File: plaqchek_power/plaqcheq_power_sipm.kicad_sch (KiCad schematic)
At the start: 20 parts

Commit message: finish schematic
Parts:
- removed U17: ~, symbol plaqchek_mlb:LM5157
- added R23 (x3): 0R, symbol Device:R_Small_US
- added TP3, TP4: TestPoint, symbol Connector:TestPoint
- added U1: LM5157, symbol plaqchek:LM5157
- R37: value 90.9kR -> 110kR
- R41: value 374R -> 464R
- R42: value 374R -> 5.1R
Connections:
- net +12V: now also R23.2; no longer C47.1, C48.2, L4.1, R43.2
- net GND: now also U1.1 (PGND), U1.16 (PGND), U1.17 (EP), U1.7 (AGND)
- net PD_BOOST_PGOOD: now also U1.4 (PGOOD)
- net PD_EN: now also R23.2
- net at R42.2: now also U1.2 (VCC)
- net at R46.2: now also U1.5 (RT)
- net at D2.2 (A), L4.2: now also U1.12 (SW), U1.13 (SW), U1.14 (SW)
- net at C52.2: now also U1.10 (SS)
- net at C50.1, C51.2: now also U1.8 (COMP)
- net at R37.2, R38.1: now also U1.9 (FB)
- net at R40.1: now also U1.11 (MODE)
- net SIPM_44V: no longer names the net of C53.2, C54.2, D2.1 (K), R37.1
- net SIPM_44V: now also R23.2, TP3.1
- new net: C47.1, C48.2, L4.1, R23.1, R43.2, U1.3 (BIAS)
- new net: R23.1, U1.6 (EN/UVLO/SYNC)
- new net SIPM_BIAS_OUT: R23.1, TP4.1
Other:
- note added: "Iout max = 500mA"
- note added: "SK220ATR"
- note removed: "B160-13-F"

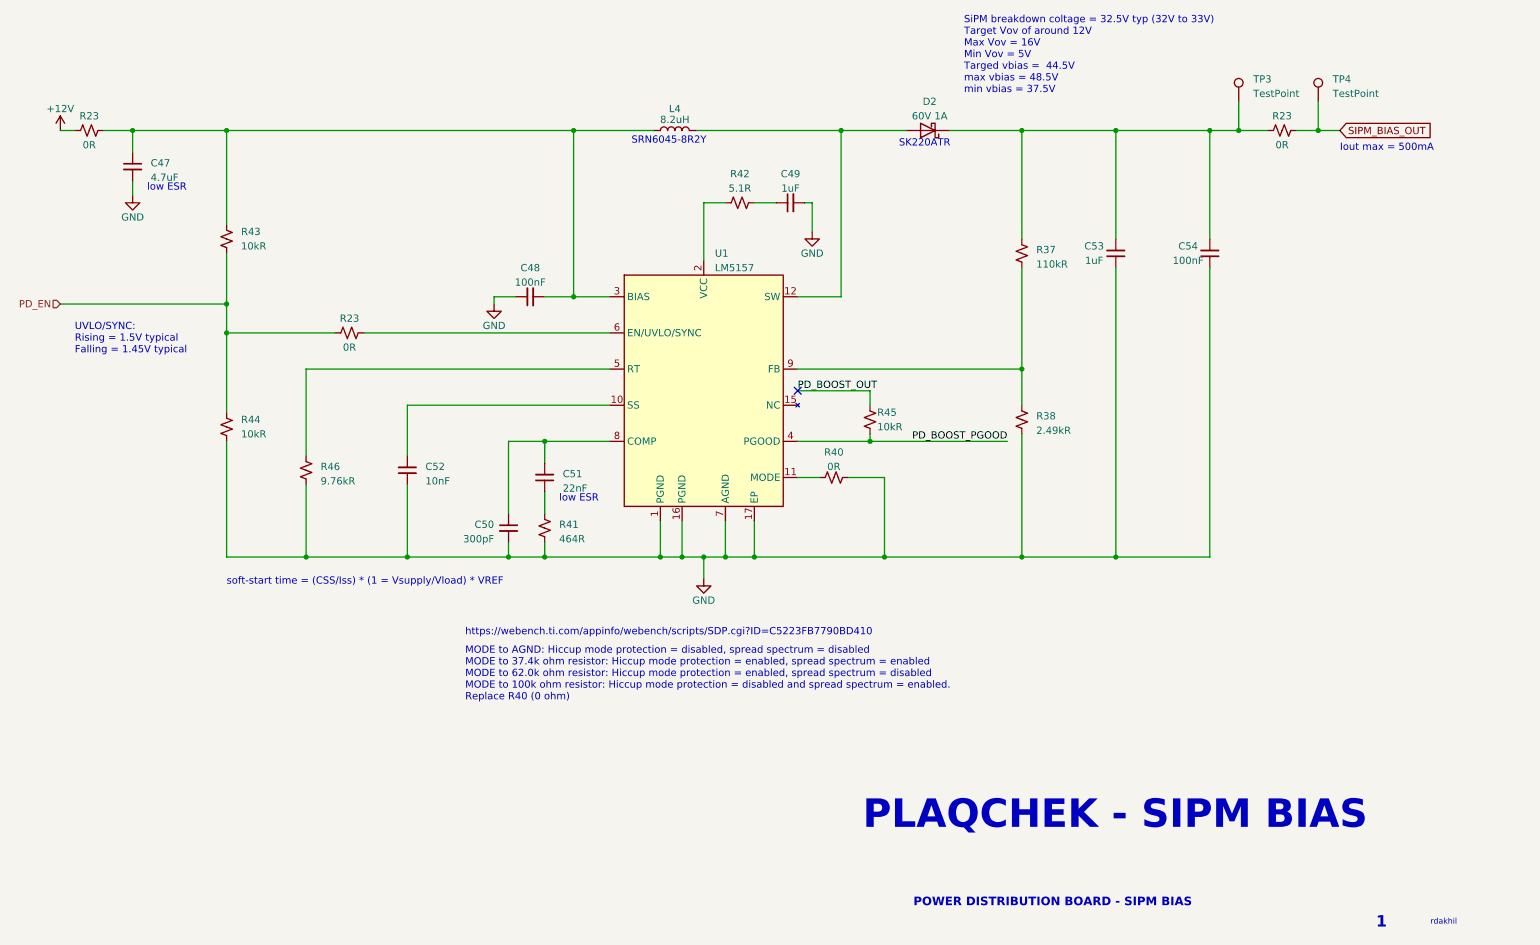
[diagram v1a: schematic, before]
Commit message: more footprints and some value fixes
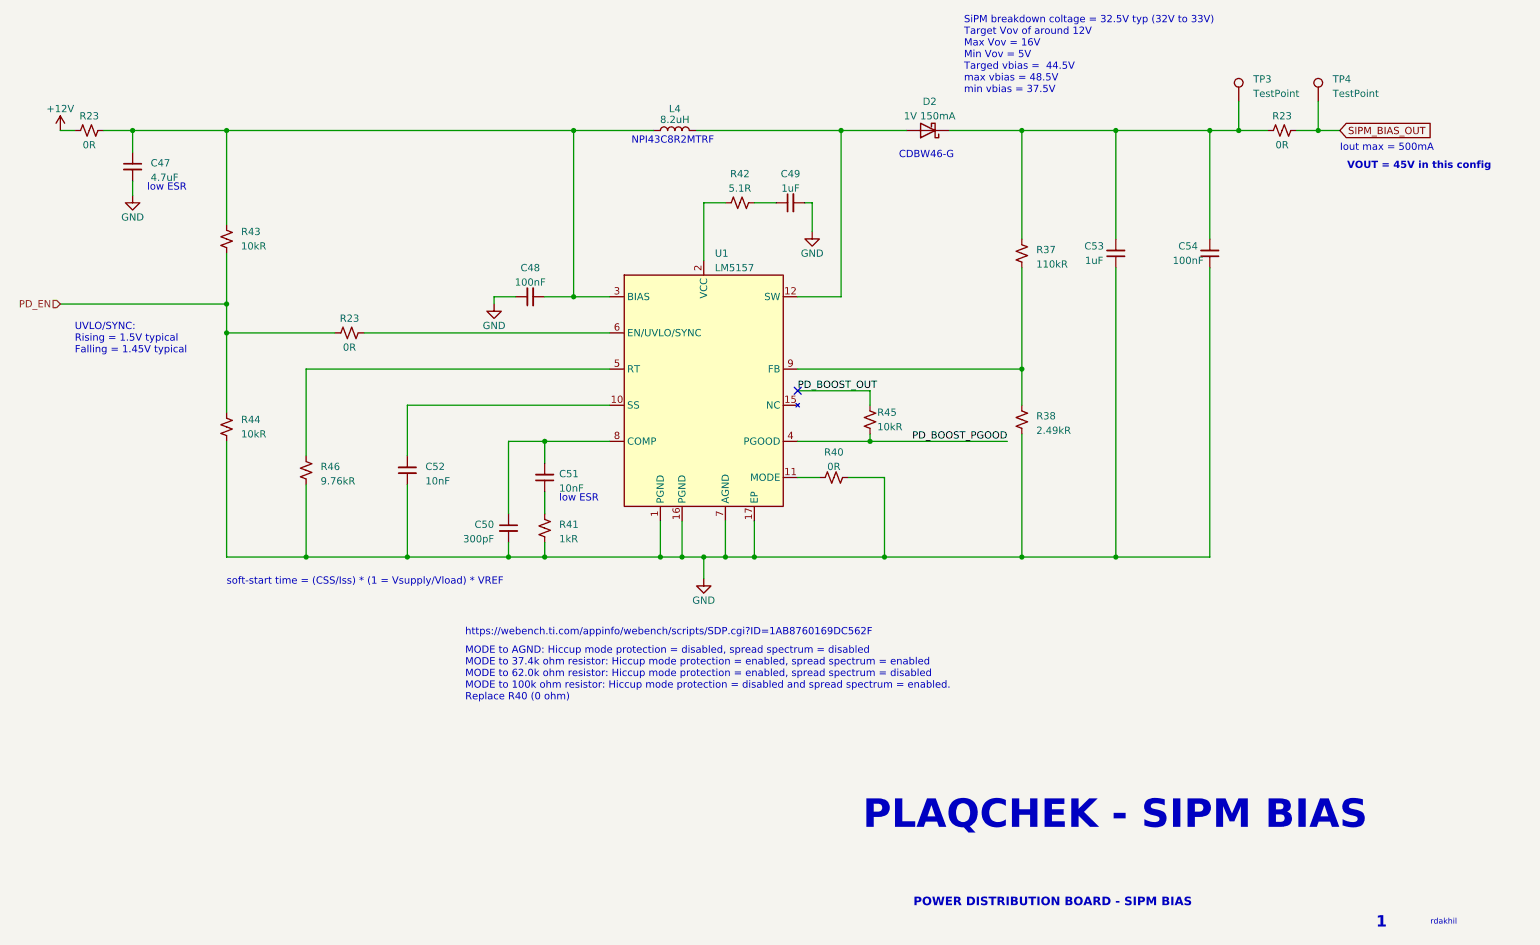
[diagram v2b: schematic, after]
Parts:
- C47, C52: footprint (none) -> Capacitor_SMD:C_0805_2012Metric_Pad1.18x1.45mm_HandSolder
- C48, C49, C50, C53, C54: footprint (none) -> Capacitor_SMD:C_0603_1608Metric_Pad1.08x0.95mm_HandSolder
- C51: value 22nF -> 10nF; footprint (none) -> Capacitor_SMD:C_0603_1608Metric_Pad1.08x0.95mm_HandSolder
- D2: value 60V 1A -> 1V 150mA
- R41: value 464R -> 1kR
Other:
- note added: "CDBW46-G"
- note added: "NPI43C8R2MTRF"
- note added: "VOUT = 45V in this config"
- note added: "https://webench.ti.com/appinfo/webench/scripts/SDP.cgi?ID=1AB8760169DC562F"
- note removed: "SK220ATR"
- note removed: "SRN6045-8R2Y"
- note removed: "https://webench.ti.com/appinfo/webench/scripts/SDP.cgi?ID=C5223FB7790BD410"
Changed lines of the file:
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@@
     (effects (font (size 2 2) (thickness 1) bold) (justify left bottom))
   )
-  (text "SK220ATR\n\n" (at 184.15 59.69 0)
+  (text "CDBW46-G\n" (at 184.15 59.69 0)
     (effects (font (size 1.27 1.27)) (justify left bottom))
   )
@@
     (effects (font (size 1.27 1.27)) (justify left bottom))
   )
-  (text "https://webench.ti.com/appinfo/webench/scripts/SDP.cgi?ID=C5223FB7790BD410"
+  (text "VOUT = 45V in this config\n" (at 262.89 61.595 0)
+    (effects (font (size 1.27 1.27) (thickness 0.254) bold) (justify left bottom))
+  )
+  (text "https://webench.ti.com/appinfo/webench/scripts/SDP.cgi?ID=1AB8760169DC562F"
     (at 107.95 143.51 0)
     (effects (font (size 1.27 1.27)) (justify left bottom))
@@
     (effects (font (size 1.5 1.5) (thickness 0.3) bold) (justify left bottom))
   )
-  (text "SRN6045-8R2Y" (at 137.16 57.15 0)
+  (text "NPI43C8R2MTRF" (at 137.16 57.15 0)
     (effects (font (size 1.27 1.27)) (justify left bottom))
   )
@@
       (effects (font (size 1.27 1.27)) (justify left))
     )
-    (property "Footprint" "" (at 49.53 60.96 0)
+    (property "Footprint" "Capacitor_SMD:C_0805_2012Metric_Pad1.18x1.45mm_HandSolder" (at 49.53 60.96 0)
       (effects (font (size 1.27 1.27)) hide)
     )
@@
       (effects (font (size 1.27 1.27)))
     )
-    (property "Footprint" "" (at 238.76 76.2 0)
+    (property "Footprint" "Capacitor_SMD:C_0603_1608Metric_Pad1.08x0.95mm_HandSolder" (at 238.76 76.2 0)
       (effects (font (size 1.27 1.27)) hide)
     )
@@
       (effects (font (size 1.27 1.27)))
     )
-    (property "Footprint" "" (at 165.1 67.31 0)
+    (property "Footprint" "Capacitor_SMD:C_0603_1608Metric_Pad1.08x0.95mm_HandSolder" (at 165.1 67.31 0)
       (effects (font (size 1.27 1.27)) hide)
     )
@@
   (symbol (lib_id "Device:C_Small") (at 121.92 115.57 180) (unit 1)
     (in_bom yes) (on_board yes) (dnp no) (fields_autoplaced)
-    (property "Reference" "C51" (at 125.095 114.9286 0)
-      (effects (font (size 1.27 1.27)) (justify right))
-    )
-    (property "Value" "22nF" (at 125.095 117.4686 0)
-      (effects (font (size 1.27 1.27)) (justify right))
-    )
-    (property "Footprint" "" (at 121.92 115.57 0)
+    (property "Reference" "C51" (at 124.46 114.9286 0)
+      (effects (font (size 1.27 1.27)) (justify right))
+    )
+    (property "Value" "10nF" (at 124.46 117.4686 0)
+      (effects (font (size 1.27 1.27)) (justify right))
+    )
+    (property "Footprint" "Capacitor_SMD:C_0603_1608Metric_Pad1.08x0.95mm_HandSolder" (at 121.92 115.57 0)
       (effects (font (size 1.27 1.27)) hide)
     )
@@
       (effects (font (size 1.27 1.27)))
     )
-    (property "Footprint" "" (at 222.25 76.2 0)
+    (property "Footprint" "Capacitor_SMD:C_0603_1608Metric_Pad1.08x0.95mm_HandSolder" (at 222.25 76.2 0)
       (effects (font (size 1.27 1.27)) hide)
     )
@@
       (effects (font (size 1.27 1.27)) (justify right))
     )
-    (property "Footprint" "" (at 97.79 114.3 0)
+    (property "Footprint" "Capacitor_SMD:C_0805_2012Metric_Pad1.18x1.45mm_HandSolder" (at 97.79 114.3 0)
       (effects (font (size 1.27 1.27)) hide)
     )
@@
       (effects (font (size 1.27 1.27)) (justify right))
     )
-    (property "Value" "464R" (at 124.46 126.365 0)
+    (property "Value" "1kR" (at 124.46 126.365 0)
       (effects (font (size 1.27 1.27)) (justify right))
     )
@@
       (effects (font (size 1.27 1.27)) (justify left))
     )
-    (property "Footprint" "" (at 115.57 124.46 0)
+    (property "Footprint" "Capacitor_SMD:C_0603_1608Metric_Pad1.08x0.95mm_HandSolder" (at 115.57 124.46 0)
       (effects (font (size 1.27 1.27)) hide)
     )
@@
       (effects (font (size 1.27 1.27)))
     )
-    (property "Value" "60V 1A" (at 189.5475 52.07 0)
+    (property "Value" "1V 150mA" (at 189.5475 52.07 0)
       (effects (font (size 1.27 1.27)))
     )
@@
       (effects (font (size 1.27 1.27)))
     )
-    (property "Footprint" "" (at 119.38 83.82 0)
-      (effects (font (size 1.27 1.27)) hide)
-    )
+    (property "Footprint" "Capacitor_SMD:C_0603_1608Metric_Pad1.08x0.95mm_HandSolder" (at 119.38 83.82 0)
+      (effects (font (size 1.27 1.27)) hide)
+    )

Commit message: finish main logic board PCB routing
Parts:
- D2: footprint (none) -> Diode_SMD:D_SOD-123
- L4: footprint (none) -> Inductor_SMD:L_1008_2520Metric_Pad1.43x2.20mm_HandSolder
- R23, R37, R38, R40, R41, R42, R43, R44, R45, R46: footprint (none) -> Resistor_SMD:R_0603_1608Metric_Pad0.98x0.95mm_HandSolder
- U1: footprint (none) -> Package_DFN_QFN:WQFN-16-1EP_3x3mm_P0.5mm_EP1.68x1.68mm
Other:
- note added: "74438323082"
- note added: "LM51571RTE"
- note removed: "NPI43C8R2MTRF"
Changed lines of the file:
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@@
     (stroke (width 0) (type default))
+  )
+  (text "LM51571RTE" (at 135.255 78.74 0)
+    (effects (font (size 1.27 1.27)) (justify left bottom))
   )
   (text "soft-start time = (CSS/Iss) * (1 = Vsupply/Vload) * VREF"
@@
     (effects (font (size 1.5 1.5) (thickness 0.3) bold) (justify left bottom))
   )
-  (text "NPI43C8R2MTRF" (at 137.16 57.15 0)
+  (text "74438323082\n" (at 137.16 57.15 0)
     (effects (font (size 1.27 1.27)) (justify left bottom))
   )
@@
       (effects (font (size 1.27 1.27)) (justify right))
     )
-    (property "Footprint" "" (at 66.04 106.68 0)
+    (property "Footprint" "Resistor_SMD:R_0603_1608Metric_Pad0.98x0.95mm_HandSolder" (at 66.04 106.68 0)
       (effects (font (size 1.27 1.27)) hide)
     )
@@
       (effects (font (size 1.27 1.27)))
     )
-    (property "Footprint" "" (at 251.46 54.61 0)
+    (property "Footprint" "Resistor_SMD:R_0603_1608Metric_Pad0.98x0.95mm_HandSolder" (at 251.46 54.61 0)
       (effects (font (size 1.27 1.27)) hide)
     )
@@
       (effects (font (size 1.27 1.27)))
     )
-    (property "Footprint" "" (at 41.91 54.61 0)
+    (property "Footprint" "Resistor_SMD:R_0603_1608Metric_Pad0.98x0.95mm_HandSolder" (at 41.91 54.61 0)
       (effects (font (size 1.27 1.27)) hide)
     )
@@
       (effects (font (size 1.27 1.27)))
     )
-    (property "Footprint" "" (at 156.21 67.31 0)
+    (property "Footprint" "Resistor_SMD:R_0603_1608Metric_Pad0.98x0.95mm_HandSolder" (at 156.21 67.31 0)
       (effects (font (size 1.27 1.27)) hide)
     )
@@
       (effects (font (size 1.27 1.27)) (justify right))
     )
-    (property "Footprint" "" (at 66.04 73.66 0)
+    (property "Footprint" "Resistor_SMD:R_0603_1608Metric_Pad0.98x0.95mm_HandSolder" (at 66.04 73.66 0)
       (effects (font (size 1.27 1.27)) hide)
     )
@@
       (effects (font (size 1.27 1.27)) (justify right))
     )
-    (property "Footprint" "" (at 80.01 114.3 0)
+    (property "Footprint" "Resistor_SMD:R_0603_1608Metric_Pad0.98x0.95mm_HandSolder" (at 80.01 114.3 0)
       (effects (font (size 1.27 1.27)) hide)
     )
@@
       (effects (font (size 1.27 1.27)) (justify right))
     )
-    (property "Footprint" "" (at 179.07 105.41 0)
+    (property "Footprint" "Resistor_SMD:R_0603_1608Metric_Pad0.98x0.95mm_HandSolder" (at 179.07 105.41 0)
       (effects (font (size 1.27 1.27)) hide)
     )
@@
       (effects (font (size 1.27 1.27)))
     )
-    (property "Footprint" "" (at 144.78 54.61 0)
+    (property "Footprint" "Inductor_SMD:L_1008_2520Metric_Pad1.43x2.20mm_HandSolder" (at 144.78 54.61 0)
       (effects (font (size 1.27 1.27)) hide)
     )
@@
       (effects (font (size 1.27 1.27)))
     )
-    (property "Footprint" "" (at 87.63 90.17 0)
+    (property "Footprint" "Resistor_SMD:R_0603_1608Metric_Pad0.98x0.95mm_HandSolder" (at 87.63 90.17 0)
       (effects (font (size 1.27 1.27)) hide)
     )
@@
       (effects (font (size 1.27 1.27)))
     )
-    (property "Footprint" "" (at 172.72 115.57 0)
+    (property "Footprint" "Resistor_SMD:R_0603_1608Metric_Pad0.98x0.95mm_HandSolder" (at 172.72 115.57 0)
       (effects (font (size 1.27 1.27)) hide)
     )
@@
       (effects (font (size 1.27 1.27)) (justify left))
     )
-    (property "Footprint" "" (at 149.86 99.06 0)
+    (property "Footprint" "Package_DFN_QFN:WQFN-16-1EP_3x3mm_P0.5mm_EP1.68x1.68mm" (at 149.86 99.06 0)
       (effects (font (size 1.27 1.27)) hide)
     )
@@
       (effects (font (size 1.27 1.27)) (justify left))
     )
-    (property "Footprint" "" (at 205.74 76.2 0)
+    (property "Footprint" "Resistor_SMD:R_0603_1608Metric_Pad0.98x0.95mm_HandSolder" (at 205.74 76.2 0)
       (effects (font (size 1.27 1.27)) hide)
     )
@@
       (effects (font (size 1.27 1.27)) (justify left))
     )
-    (property "Footprint" "" (at 205.74 105.41 0)
+    (property "Footprint" "Resistor_SMD:R_0603_1608Metric_Pad0.98x0.95mm_HandSolder" (at 205.74 105.41 0)
       (effects (font (size 1.27 1.27)) hide)
     )
@@
       (effects (font (size 1.27 1.27)) (justify right))
     )
-    (property "Footprint" "" (at 121.92 124.46 0)
+    (property "Footprint" "Resistor_SMD:R_0603_1608Metric_Pad0.98x0.95mm_HandSolder" (at 121.92 124.46 0)
       (effects (font (size 1.27 1.27)) hide)
     )
@@
       (effects (font (size 1.27 1.27)))
     )
-    (property "Footprint" "" (at 189.23 54.61 0)
-      (effects (font (size 1.27 1.27)) hide)
-    )
+    (property "Footprint" "Diode_SMD:D_SOD-123" (at 189.23 54.61 0)
+      (effects (font (size 1.27 1.27)) hide)
+    )
